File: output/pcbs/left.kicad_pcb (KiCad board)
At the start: 2 copper layers, 138.6 x 90.9 mm, 19 parts

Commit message: adds footprints
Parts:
- added B1: Panasonic_EVQPUL_EVQPUC, Panasonic_EVQPUL_EVQPUC, F.Cu at (204.0, 140.0)
- added D1: , ComboDiode, F.Cu at (107.8, 153.5)
- added D10: , ComboDiode, F.Cu at (161.1, 145.5)
- added D11: , ComboDiode, F.Cu at (161.1, 126.8)
- added D12: , ComboDiode, F.Cu at (161.1, 108.0)
- added D13: , ComboDiode, F.Cu at (178.8, 146.5)
- added D14: , ComboDiode, F.Cu at (178.8, 127.8)
- added D15: , ComboDiode, F.Cu at (178.8, 109.0)
- added D16: , ComboDiode, F.Cu at (167.8, 166.7)
- added D17: , ComboDiode, F.Cu at (193.2, 173.7)
- added D18: , ComboDiode, F.Cu at (220.4, 184.3)
- added D2: , ComboDiode, F.Cu at (107.8, 134.8)
- added D3: , ComboDiode, F.Cu at (107.8, 116.0)
- added D4: , ComboDiode, F.Cu at (125.5, 145.5)
- added D5: , ComboDiode, F.Cu at (125.5, 126.8)
- added D6: , ComboDiode, F.Cu at (125.5, 108.0)
- added D7: , ComboDiode, F.Cu at (143.3, 143.0)
- added D8: , ComboDiode, F.Cu at (143.3, 124.2)
- added D9: , ComboDiode, F.Cu at (143.3, 105.5)
- added JST1: , JST_PH_S2B-PH-K_02x2.00mm_Angled, F.Cu at (209.8, 137.0)
- added T1: , E73:SPDT_C128955, F.Cu at (204.0, 144.0)
- moved S18 180.9 mm to (214.8, 177.8)
- moved S1 180.3 mm to (100.0, 150.0)
- moved S4 180.1 mm to (117.8, 142.0)
- moved S7 180.0 mm to (135.5, 139.5)
- moved S10 179.9 mm to (153.2, 142.0)
- moved S13 179.7 mm to (171.0, 143.0)
- moved S2 178.8 mm to (100.0, 131.2)
- moved S5 178.7 mm to (117.8, 123.2)
- moved S8 178.5 mm to (135.5, 120.8)
- moved MCU1 178.5 mm to (193.0, 115.5)
- moved S11 178.4 mm to (153.2, 123.2)
- moved S16 178.4 mm to (160.0, 163.2)
- moved S17 178.4 mm to (187.1, 167.7)
- moved S14 178.3 mm to (171.0, 124.2)
- moved S3 177.4 mm to (100.0, 112.5)
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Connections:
- S1 pad 1: (no net) -> P020
- S10 pad 1: (no net) -> P100
- S11 pad 1: (no net) -> P100
- S12 pad 1: (no net) -> P100
- S13 pad 1: (no net) -> P011
- S14 pad 1: (no net) -> P011
- S15 pad 1: (no net) -> P011
- S16 pad 1: (no net) -> P111
- S17 pad 1: (no net) -> P009
- S18 pad 1: (no net) -> P010
- S2 pad 1: (no net) -> P020
- S3 pad 1: (no net) -> P020
- S4 pad 1: (no net) -> P022
- S5 pad 1: (no net) -> P022
- S6 pad 1: (no net) -> P022
- S7 pad 1: (no net) -> P024
- S8 pad 1: (no net) -> P024
- S9 pad 1: (no net) -> P024
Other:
- board size 138.6 x 90.9 mm -> 76 x 92.8 mm
- board text added: "ARC-T"

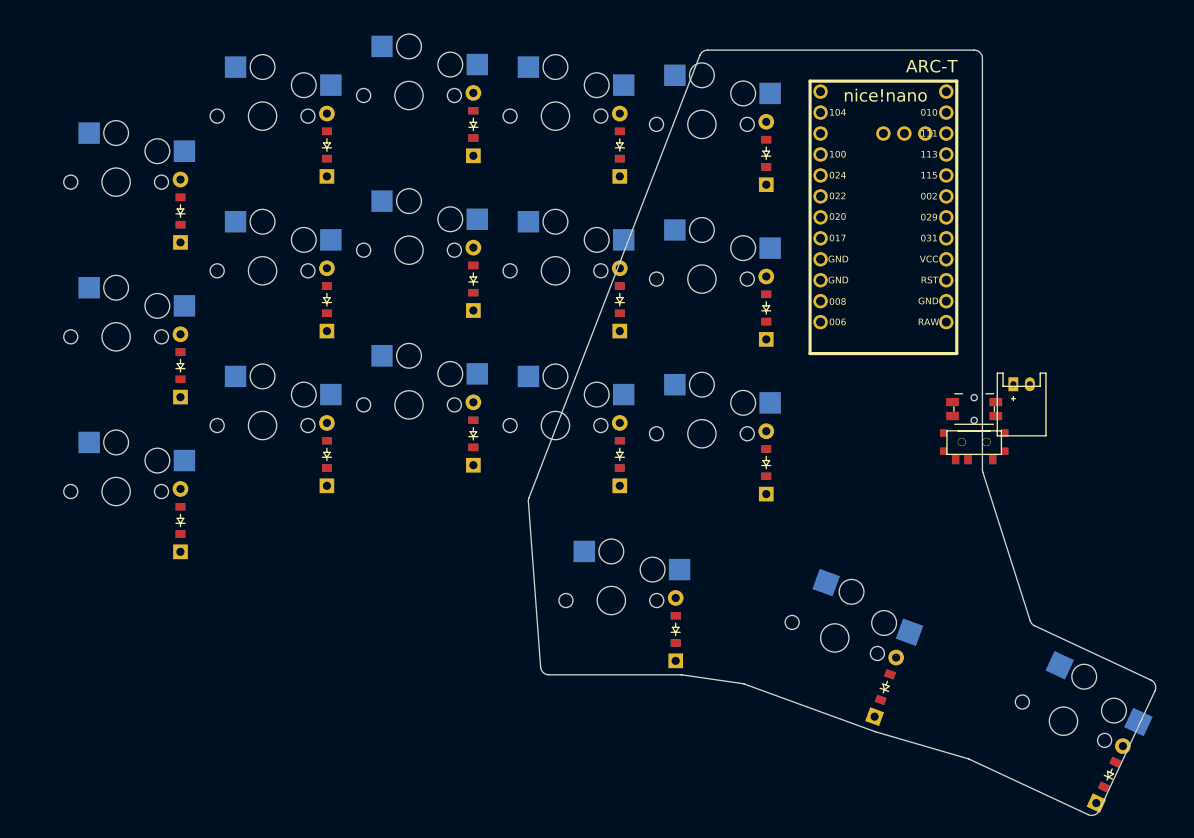
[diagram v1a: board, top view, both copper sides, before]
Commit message: tiding up in the upper portion of border
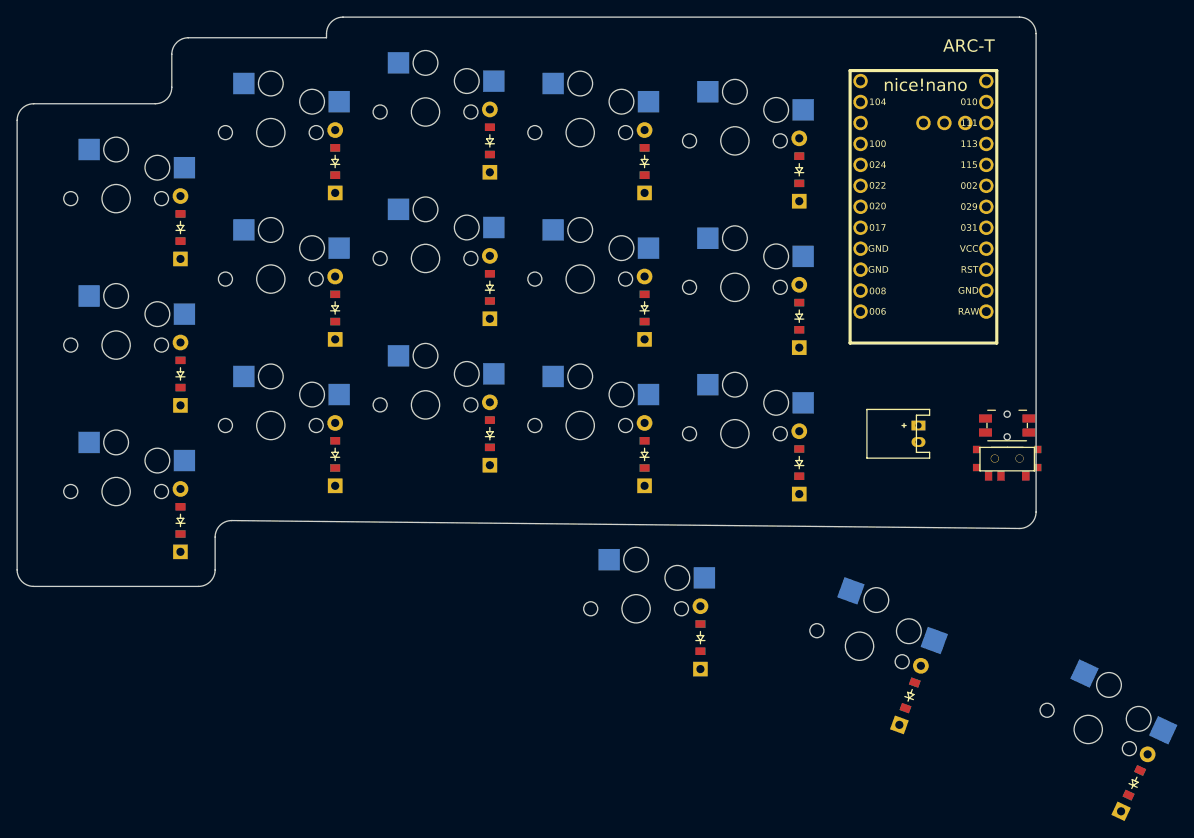
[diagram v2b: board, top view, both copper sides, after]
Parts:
- moved JST1 13.9 mm to (197.2, 143.0), turned to -90 degrees
- moved MCU1 5.02 mm to (197.8, 114.2)
- moved B1 4.47 mm to (208.0, 142.0)
- moved D15 4.47 mm to (182.8, 111.0)
- moved S15 4.47 mm to (175.0, 107.5)
- moved T1 4.47 mm to (208.0, 146.0)
- moved D14 4.12 mm to (182.8, 128.8)
- moved S14 4.12 mm to (175.0, 125.2)
- moved D13 4.00 mm to (182.8, 146.5)
- moved S13 4.00 mm to (175.0, 143.0)
- moved D12 3.61 mm to (164.1, 110.0)
- moved S12 3.61 mm to (156.2, 106.5)
- moved D11 3.16 mm to (164.1, 127.8)
- moved D16 3.16 mm to (170.8, 167.7)
- moved D17 3.16 mm to (196.2, 174.7)
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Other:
- board size 76 x 92.8 mm -> 123.5 x 69 mm

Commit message: v1 design
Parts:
- moved JST1 6.12 mm to (203.4, 143.0)
- moved T1 5.61 mm to (209.1, 151.5), turned to -90 degrees
- moved B1 1.51 mm to (209.1, 143.0), turned to -90 degrees
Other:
- board size 123.5 x 69 mm -> 144.9 x 101.3 mm
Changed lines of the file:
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@@
         (descr "JST PH series connector, S2B-PH-K, side entry type, through hole, Datasheet: http://www.jst-mfg.com/product/pdf/eng/ePH.pdf")
         (tags "connector jst ph")
-        (at 197.25 143 -90)
+        (at 203.375 143 -90)
         (fp_text reference "JST1" (at 0 0) (layer F.SilkS) hide (effects (font (size 1.27 1.27) (thickness 0.15))))
         (fp_text value "" (at 0 0) (layer F.SilkS) hide (effects (font (size 1.27 1.27) (thickness 0.15))))
@@
         (descr "http://industrial.panasonic.com/cdbs/www-data/pdf/ATV0000/ATV0000CE5.pdf")
         (tags "SMD SMT SPST EVQPUL EVQPUC")
-        (at 208 142 0)
+        (at 209.125 143 -90)
         (fp_text reference "B1" (at 0 0) (layer "F.SilkS") hide (effects (font (size 1 1) (thickness 0.15))))
         (fp_text value "Panasonic_EVQPUL_EVQPUC" (at 0 3.5) (layer "F.Fab") hide (effects (font (size 1 1) (thickness 0.15))))
@@
         (fp_line (start 2.35 1.75) (end -2.35 1.75) (stroke (width 0.1) (type solid)) (layer "F.Fab"))
         (fp_line (start 2.35 1.75) (end 2.35 -1.75) (stroke (width 0.1) (type solid)) (layer "F.Fab"))
-        (pad "" np_thru_hole circle (at 0 -1.375 0) (size 0.75 0.75) (drill 0.75) (layers "*.Cu" "*.Mask"))
-        (pad "" np_thru_hole circle (at 0 1.375 0) (size 0.75 0.75) (drill 0.75) (layers "*.Cu" "*.Mask"))
-        (pad "1" smd rect (at -2.625 -0.85 0) (size 1.55 1) (layers "F.Cu" "F.Paste" "F.Mask") (net 32 "GND"))
-        (pad "1" smd rect (at 2.625 -0.85 0) (size 1.55 1) (layers "F.Cu" "F.Paste" "F.Mask") (net 32 "GND"))
-        (pad "2" smd rect (at -2.625 0.85 0) (size 1.55 1) (layers "F.Cu" "F.Paste" "F.Mask") (net 33 "RST"))
-        (pad "2" smd rect (at 2.625 0.85 0) (size 1.55 1) (layers "F.Cu" "F.Paste" "F.Mask") (net 33 "RST"))
+        (pad "" np_thru_hole circle (at 0 -1.375 -90) (size 0.75 0.75) (drill 0.75) (layers "*.Cu" "*.Mask"))
+        (pad "" np_thru_hole circle (at 0 1.375 -90) (size 0.75 0.75) (drill 0.75) (layers "*.Cu" "*.Mask"))
+        (pad "1" smd rect (at -2.625 -0.85 -90) (size 1.55 1) (layers "F.Cu" "F.Paste" "F.Mask") (net 32 "GND"))
+        (pad "1" smd rect (at 2.625 -0.85 -90) (size 1.55 1) (layers "F.Cu" "F.Paste" "F.Mask") (net 32 "GND"))
+        (pad "2" smd rect (at -2.625 0.85 -90) (size 1.55 1) (layers "F.Cu" "F.Paste" "F.Mask") (net 33 "RST"))
+        (pad "2" smd rect (at 2.625 0.85 -90) (size 1.55 1) (layers "F.Cu" "F.Paste" "F.Mask") (net 33 "RST"))
     )
         (module E73:SPDT_C128955 (layer F.Cu)
-            (at 208 146 0)
+            (at 209.125 151.5 -90)
             (fp_text reference "T1" (at 0 0) (layer F.SilkS) hide (effects (font (size 1.27 1.27) (thickness 0.15))))
             (fp_text value "" (at 0 0) (layer F.SilkS) hide (effects (font (size 1.27 1.27) (thickness 0.15))))
@@
             (pad "" np_thru_hole circle (at 1.5 0) (size 1 1) (drill 0.9) (layers *.Cu *.Mask))
             (pad "" np_thru_hole circle (at -1.5 0) (size 1 1) (drill 0.9) (layers *.Cu *.Mask))
-            (pad 1 smd rect (at 2.25 2.075 0) (size 0.9 1.25) (layers F.Cu F.Paste F.Mask) (net 31 "pos"))
-            (pad 2 smd rect (at -0.75 2.075 0) (size 0.9 1.25) (layers F.Cu F.Paste F.Mask) (net 34 "RAW"))
-            (pad 3 smd rect (at -2.25 2.075 0) (size 0.9 1.25) (layers F.Cu F.Paste F.Mask))
-            (pad "" smd rect (at 3.7 -1.1 0) (size 0.9 0.9) (layers F.Cu F.Paste F.Mask))
-            (pad "" smd rect (at 3.7 1.1 0) (size 0.9 0.9) (layers F.Cu F.Paste F.Mask))
-            (pad "" smd rect (at -3.7 1.1 0) (size 0.9 0.9) (layers F.Cu F.Paste F.Mask))
-            (pad "" smd rect (at -3.7 -1.1 0) (size 0.9 0.9) (layers F.Cu F.Paste F.Mask))
+            (pad 1 smd rect (at 2.25 2.075 -90) (size 0.9 1.25) (layers F.Cu F.Paste F.Mask) (net 31 "pos"))
+            (pad 2 smd rect (at -0.75 2.075 -90) (size 0.9 1.25) (layers F.Cu F.Paste F.Mask) (net 34 "RAW"))
+            (pad 3 smd rect (at -2.25 2.075 -90) (size 0.9 1.25) (layers F.Cu F.Paste F.Mask))
+            (pad "" smd rect (at 3.7 -1.1 -90) (size 0.9 0.9) (layers F.Cu F.Paste F.Mask))
+            (pad "" smd rect (at 3.7 1.1 -90) (size 0.9 0.9) (layers F.Cu F.Paste F.Mask))
+            (pad "" smd rect (at -3.7 1.1 -90) (size 0.9 0.9) (layers F.Cu F.Paste F.Mask))
+            (pad "" smd rect (at -3.7 -1.1 -90) (size 0.9 0.9) (layers F.Cu F.Paste F.Mask))
         )
       (module nice_nano (layer F.Cu)
@@
                 (effects (font (size 1.5 1.5) (thickness 0.2) ) (justify right))
             )
-  (gr_line (start 114.0200994000101 153.52030250653277) (end 209.47990059998992 154.47969749346723) (angle 90) (layer Edge.Cuts) (width 0.15))
-(gr_line (start 211.5 152.4797984924623) (end 211.5 94.5) (angle 90) (layer Edge.Cuts) (width 0.15))
+  (gr_line (start 231.76792644501444 172.63455156287586) (end 212.64135656122573 163.5425546945115) (angle 90) (layer Edge.Cuts) (width 0.15))
+(gr_line (start 211.5 161.7362514129432) (end 211.5 94.5) (angle 90) (layer Edge.Cuts) (width 0.15))
 (gr_line (start 127.5 92.5) (end 209.5 92.5) (angle 90) (layer Edge.Cuts) (width 0.15))
 (gr_line (start 125.5 94.5) (end 125.5 95) (angle 90) (layer Edge.Cuts) (width 0.15))
@@
 (gr_line (start 88 105) (end 88 159.5) (angle 90) (layer Edge.Cuts) (width 0.15))
 (gr_line (start 90 161.5) (end 110 161.5) (angle 90) (layer Edge.Cuts) (width 0.15))
-(gr_line (start 112 159.5) (end 112 155.52020150753768) (angle 90) (layer Edge.Cuts) (width 0.15))
-(gr_arc (start 209.5 152.4797984924623) (end 209.4799006 154.4796974924623) (angle -90.57581508848011) (layer Edge.Cuts) (width 0.15))
+(gr_line (start 112 159.5) (end 112 155.499861729862) (angle 90) (layer Edge.Cuts) (width 0.15))
+(gr_line (start 113.99986179999999 153.4998617298551) (end 149.02222010000003 153.49744028925517) (angle 90) (layer Edge.Cuts) (width 0.15))
+(gr_line (start 151.0223583 155.49744028926207) (end 151.0223583 173.712302) (angle 90) (layer Edge.Cuts) (width 0.15))
+(gr_line (start 153.0223583 175.712302) (end 174.67846214503413 175.712302) (angle 90) (layer Edge.Cuts) (width 0.15))
+(gr_line (start 175.34650314503415 175.8271704) (end 197.40603667205184 183.64448836699808) (angle 90) (layer Edge.Cuts) (width 0.15))
+(gr_line (start 197.48776485799797 183.67547700175254) (end 222.08063107936582 193.62021761353702) (angle 90) (layer Edge.Cuts) (width 0.15))
+(gr_line (start 224.6430158270097 192.61131123043083) (end 232.72189856793798 175.28609142658343) (angle 90) (layer Edge.Cuts) (width 0.15))
+(gr_arc (start 213.5 161.7362514129432) (end 211.5 161.7362514129432) (angle -64.57547788766138) (layer Edge.Cuts) (width 0.15))
 (gr_arc (start 209.5 94.5) (end 211.5 94.5) (angle -90) (layer Edge.Cuts) (width 0.15))
 (gr_arc (start 127.5 94.5) (end 127.5 92.5) (angle -90) (layer Edge.Cuts) (width 0.15))
@@
 (gr_arc (start 90 159.5) (end 88 159.5) (angle -90) (layer Edge.Cuts) (width 0.15))
 (gr_arc (start 110 159.5) (end 110 161.5) (angle -90) (layer Edge.Cuts) (width 0.15))
-(gr_arc (start 114 155.52020150753768) (end 114.0200994 153.52030250753768) (angle -90.57581508848052) (layer Edge.Cuts) (width 0.15))
+(gr_arc (start 114 155.499861729862) (end 113.9998618 153.499861729862) (angle -89.99604086164172) (layer Edge.Cuts) (width 0.15))
+(gr_arc (start 149.0223583 155.49744028926207) (end 151.0223583 155.49744028926207) (angle -90.00395913835747) (layer Edge.Cuts) (width 0.15))
+(gr_arc (start 153.0223583 173.712302) (end 151.0223583 173.712302) (angle -90) (layer Edge.Cuts) (width 0.15))
+(gr_arc (start 174.67846214503413 177.712302) (end 175.34650314503412 175.8271704) (angle -19.512986252304387) (layer Edge.Cuts) (width 0.15))
+(gr_arc (start 196.73799567205185 185.5296199669981) (end 197.48776487205186 183.6754769669981) (angle -2.5041940005036736) (layer Edge.Cuts) (width 0.15))
+(gr_arc (start 222.83040026531194 191.7660746482915) (end 222.08063106531193 193.6202176482915) (angle -87.01717857999182) (layer Edge.Cuts) (width 0.15))
+(gr_arc (start 230.90928300624017 174.44085484444406) (end 232.72189850624017 175.28609144444405) (angle -89.57547956047577) (layer Edge.Cuts) (width 0.15))
 )
